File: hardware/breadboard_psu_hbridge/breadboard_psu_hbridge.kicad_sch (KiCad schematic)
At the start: 39 parts, among them J1 USB_B_Micro, J2 PWR Header, J21 Breadboard Rail, J22 Breadboard Rail, J3 HV Jumper, J31 Breadboard NC, J32 Breadboard NC, J4 Filament Jumper, J5 Filament EN, J6 HV EN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

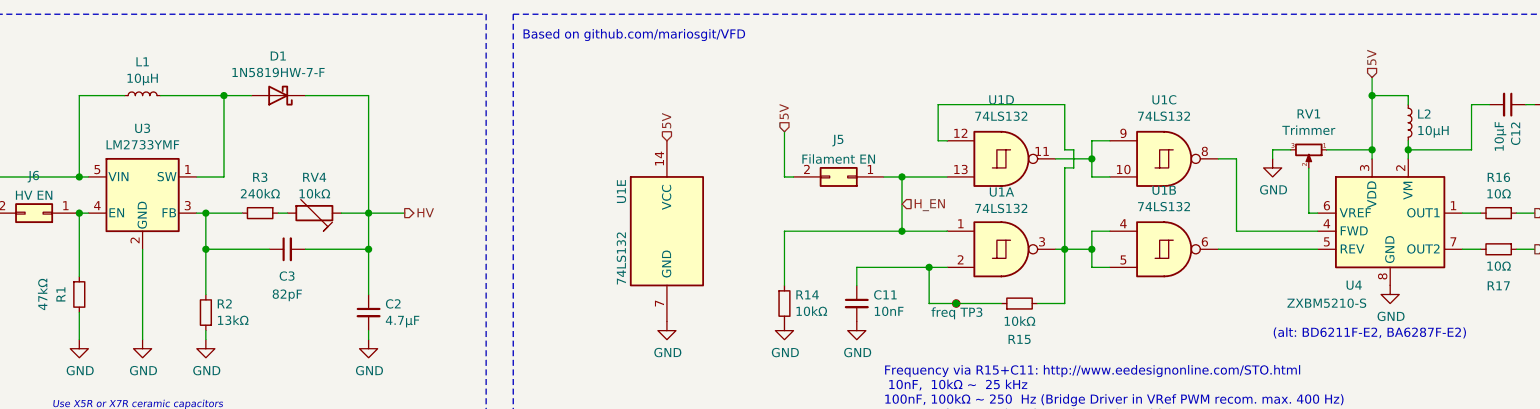
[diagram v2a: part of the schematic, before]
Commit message: hw: update breadboard hbridge psu to kicad 6
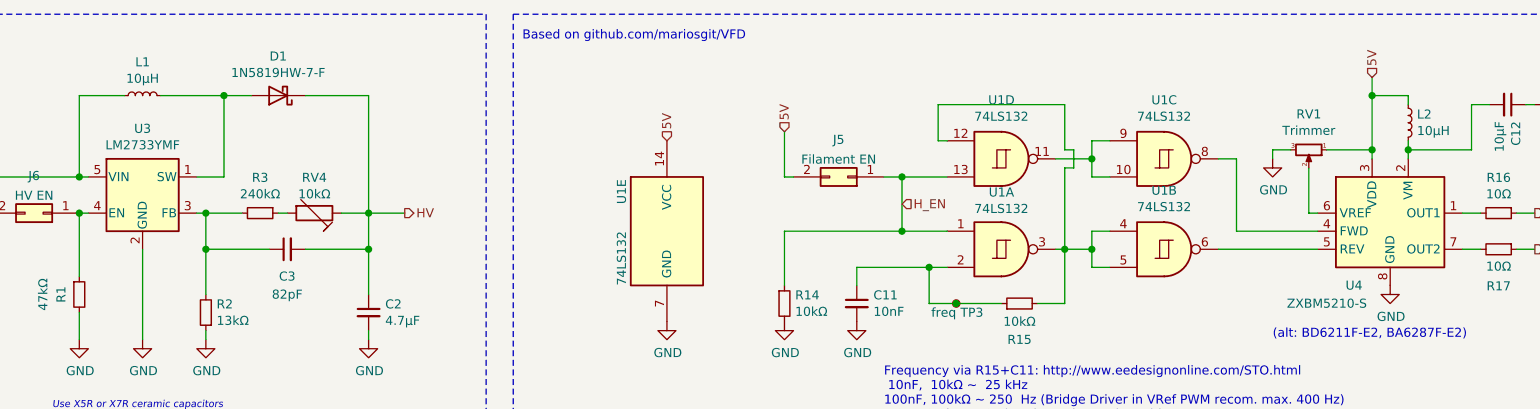
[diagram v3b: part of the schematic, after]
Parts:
- C1, C2, C3: footprint Capacitor_SMD:C_0805_2012Metric_Pad1.15x1.40mm_HandSolder -> Capacitor_SMD:C_0805_2012Metric_Pad1.18x1.45mm_HandSolder
- J1: footprint digikey-footprints:USB_Micro_B_Female_10118194-0001LF -> Connector_USB:USB_Micro-B_Amphenol_10118194_Horizontal
- R1, R2, R3: footprint Resistor_SMD:R_0805_2012Metric_Pad1.15x1.40mm_HandSolder -> Resistor_SMD:R_0805_2012Metric_Pad1.20x1.40mm_HandSolder
